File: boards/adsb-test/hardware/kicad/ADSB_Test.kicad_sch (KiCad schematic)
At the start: 0 parts

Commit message: Release v0.21.0: WT01P4C5-S1 module (P4+C5) and DS3231M RTC for ADSB_Test
Co-Authored-By: Claude Opus 5.5 <noreply@anthropic.com>
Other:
- sheet ESP32-C5 renamed RTC
- sheet ESP32-P4 renamed MCU Module
- sheet MCU Module: file esp32p4.kicad_sch -> mcu_module.kicad_sch
- sheet RTC: file esp32c5.kicad_sch -> rtc.kicad_sch
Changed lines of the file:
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@@
 			(color 0 0 0 0)
 		)
-		(property "Sheetname" "ESP32-C5"
+		(property "Sheetname" "RTC"
 			(at 125 102.3 0)
 			(show_name no)
@@
 			)
 		)
-		(property "Sheetfile" "esp32c5.kicad_sch"
+		(property "Sheetfile" "rtc.kicad_sch"
 			(at 125 128.6 0)
 			(show_name no)
@@
 			(color 0 0 0 0)
 		)
-		(property "Sheetname" "ESP32-P4"
+		(property "Sheetname" "MCU Module"
 			(at 30 102.3 0)
 			(show_name no)
@@
 			)
 		)
-		(property "Sheetfile" "esp32p4.kicad_sch"
+		(property "Sheetfile" "mcu_module.kicad_sch"
 			(at 30 128.6 0)
 			(show_name no)

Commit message: ADSB_Test: User USB-C on its own sheet, RP2040 GPIO header + optional I2C, shunt/PWR_FLAG text fixed
Co-Authored-By: Claude Opus 5.5 <noreply@anthropic.com>
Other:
- sheet USB User renamed User USB-C
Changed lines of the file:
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@@
 			(color 0 0 0 0)
 		)
-		(property "Sheetname" "USB User"
+		(property "Sheetname" "User USB-C"
 			(at 315 102.3 0)
 			(show_name no)

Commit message: ADSB_Test: Dev port split over three A3 sheets; old note boxes replaced with short current notes
Co-Authored-By: Claude Opus 5.5 <noreply@anthropic.com>
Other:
- sheet USB Dev renamed Dev USB Hub
- added sheet Dev UARTs (dev_uart.kicad_sch)
- added sheet Dev m1421 Programmer (dev_prog.kicad_sch)
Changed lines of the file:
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@@
 		(comment 1 "ESP32-P4 ADS-B test board, derived from Waveshare ESP32-P4-WIFI6-Touch-LCD-7B-C")
 	)
-	(text_box "ADSB_Test Rev A - hierarchy overview\nESP32-P4 + ESP32-C5 (Wi-Fi remote), Ethernet, User USB-C (PD sink + user UART), Dev USB-C (hub: P4 USB-JTAG, FT2232H P4+C5 UARTs, RP2040 probe for m1421),\nADSBee m1421 (1090 + 978 MHz), USB-A host (ext. hub, 1-2 SDR), GPS, 2S Li-ion + charger, V/I monitoring on every rail, 7in display + touch, microSD, LA5016 header.\nDocs: boards/adsb-test/docs (requirements, architecture, open questions, test plan)."
+	(text_box "ADSB_Test Rev A - hierarchy overview\nOSPTEK ESP32-P4C5 module (P4 + C5 Wi-Fi 6 over SDIO), Ethernet (LAN8720A), User USB-C (PD sink + user UART), Dev USB-C (hub:\nP4 USB-Serial/JTAG, FT2232H P4 + C5 consoles, RP2040 ADSBee Programmer for the m1421), ADSBee m1421 (1090 + 978 MHz),\nUSB-A host (external hub, SDRs), GPS, 2S Li-ion + BQ25798 charger, V/I monitoring on every rail, 7in display + touch,\nmicroSD, LA5016 header. Sheets are generated by boards/adsb-test/hardware/gen; docs in boards/adsb-test/docs."
 		(exclude_from_sim no)
 		(at 20 20 0)
@@
 	)
 	(sheet
+		(at 315 189)
+		(size 60 25)
+		(exclude_from_sim no)
+		(in_bom yes)
+		(on_board yes)
+		(dnp no)
+		(stroke
+			(width 0.1524)
+			(type solid)
+		)
+		(fill
+			(color 0 0 0 0)
+		)
+		(property "Sheetname" "Dev UARTs"
+			(at 315 188.3 0)
+			(show_name no)
+			(do_not_autoplace no)
+			(effects
+				(font
+					(size 1.5 1.5)
+				)
+				(justify left bottom)
+			)
+		)
+		(property "Sheetfile" "dev_uart.kicad_sch"
+			(at 315 214.6 0)
+			(show_name no)
+			(do_not_autoplace no)
+			(effects
+				(font
+					(size 1.27 1.27)
+				)
+				(justify left top)
+			)
+		)
+		(instances
+			(project "ADSB_Test"
+				(path "/3d3fb581-a5b5-4e02-aee4-847f5ac173a8"
+					(page "17")
+				)
+			)
+		)
+	)
+	(sheet
+		(at 30 232)
+		(size 60 25)
+		(exclude_from_sim no)
+		(in_bom yes)
+		(on_board yes)
+		(dnp no)
+		(stroke
+			(width 0.1524)
+			(type solid)
+		)
+		(fill
+			(color 0 0 0 0)
+		)
+		(property "Sheetname" "Dev m1421 Programmer"
+			(at 30 231.3 0)
+			(show_name no)
+			(do_not_autoplace no)
+			(effects
+				(font
+					(size 1.5 1.5)
+				)
+				(justify left bottom)
+			)
+		)
+		(property "Sheetfile" "dev_prog.kicad_sch"
+			(at 30 257.6 0)
+			(show_name no)
+			(do_not_autoplace no)
+			(effects
+				(font
+					(size 1.27 1.27)
+				)
+				(justify left top)
+			)
+		)
+		(instances
+			(project "ADSB_Test"
+				(path "/3d3fb581-a5b5-4e02-aee4-847f5ac173a8"
+					(page "18")
+				)
+			)
+		)
+	)
+	(sheet
 		(at 315 60)
 		(size 60 25)
@@
 			(color 0 0 0 0)
 		)
-		(property "Sheetname" "USB Dev"
+		(property "Sheetname" "Dev USB Hub"
 			(at 30 145.3 0)
 			(show_name no)

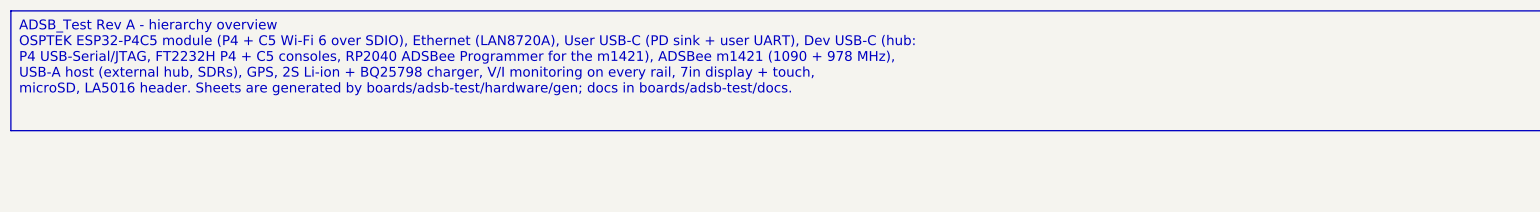
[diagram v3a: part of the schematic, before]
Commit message: ADSB_Test: Kelvin shunt footprint, Wi-Fi RP-SMA on the top edge, PCB parity 0
- Shunts RS201-RS409: 4-pad R_Shunt_1206_Kelvin_HandSolder (net-tied sense
  pads) replaces the 2-pad 1206, which put the sense net on the load pad.
- Wi-Fi: module IPEX -> U.FL jumper -> J601 -> J602 RP-SMA on the top long
  edge, away from the 1090/978 and GNSS SMAs. BOM, datasheets, docs.
- gen_pcb: symbol fields and BOM flags copied to footprints, unconnected
  net names escaped; top-edge placement.

Co-Authored-By: Claude Opus 5.5 <noreply@anthropic.com>
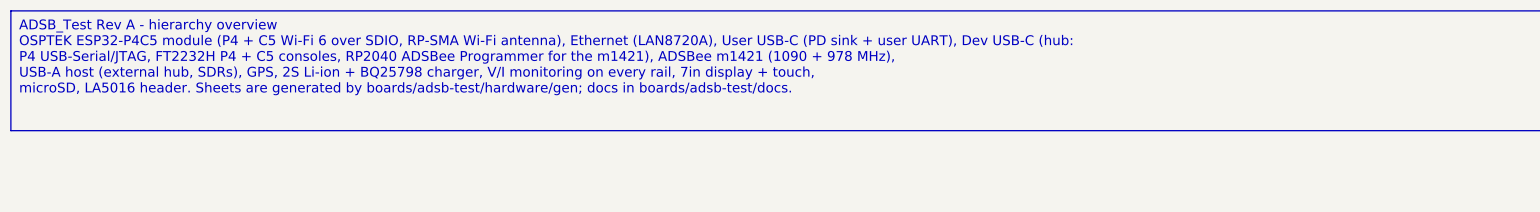
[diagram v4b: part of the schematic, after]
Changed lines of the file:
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@@
 		(comment 1 "ESP32-P4 ADS-B test board, derived from Waveshare ESP32-P4-WIFI6-Touch-LCD-7B-C")
 	)
-	(text_box "ADSB_Test Rev A - hierarchy overview\nOSPTEK ESP32-P4C5 module (P4 + C5 Wi-Fi 6 over SDIO), Ethernet (LAN8720A), User USB-C (PD sink + user UART), Dev USB-C (hub:\nP4 USB-Serial/JTAG, FT2232H P4 + C5 consoles, RP2040 ADSBee Programmer for the m1421), ADSBee m1421 (1090 + 978 MHz),\nUSB-A host (external hub, SDRs), GPS, 2S Li-ion + BQ25798 charger, V/I monitoring on every rail, 7in display + touch,\nmicroSD, LA5016 header. Sheets are generated by boards/adsb-test/hardware/gen; docs in boards/adsb-test/docs."
+	(text_box "ADSB_Test Rev A - hierarchy overview\nOSPTEK ESP32-P4C5 module (P4 + C5 Wi-Fi 6 over SDIO, RP-SMA Wi-Fi antenna), Ethernet (LAN8720A), User USB-C (PD sink + user UART), Dev USB-C (hub:\nP4 USB-Serial/JTAG, FT2232H P4 + C5 consoles, RP2040 ADSBee Programmer for the m1421), ADSBee m1421 (1090 + 978 MHz),\nUSB-A host (external hub, SDRs), GPS, 2S Li-ion + BQ25798 charger, V/I monitoring on every rail, 7in display + touch,\nmicroSD, LA5016 header. Sheets are generated by boards/adsb-test/hardware/gen; docs in boards/adsb-test/docs."
 		(exclude_from_sim no)
 		(at 20 20 0)
